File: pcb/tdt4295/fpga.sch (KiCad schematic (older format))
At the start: 45 parts, among them J101 FPGA__debug, U101 S25FL127SABMFV101, U102 XC7A100T-FTG256-tdt4295

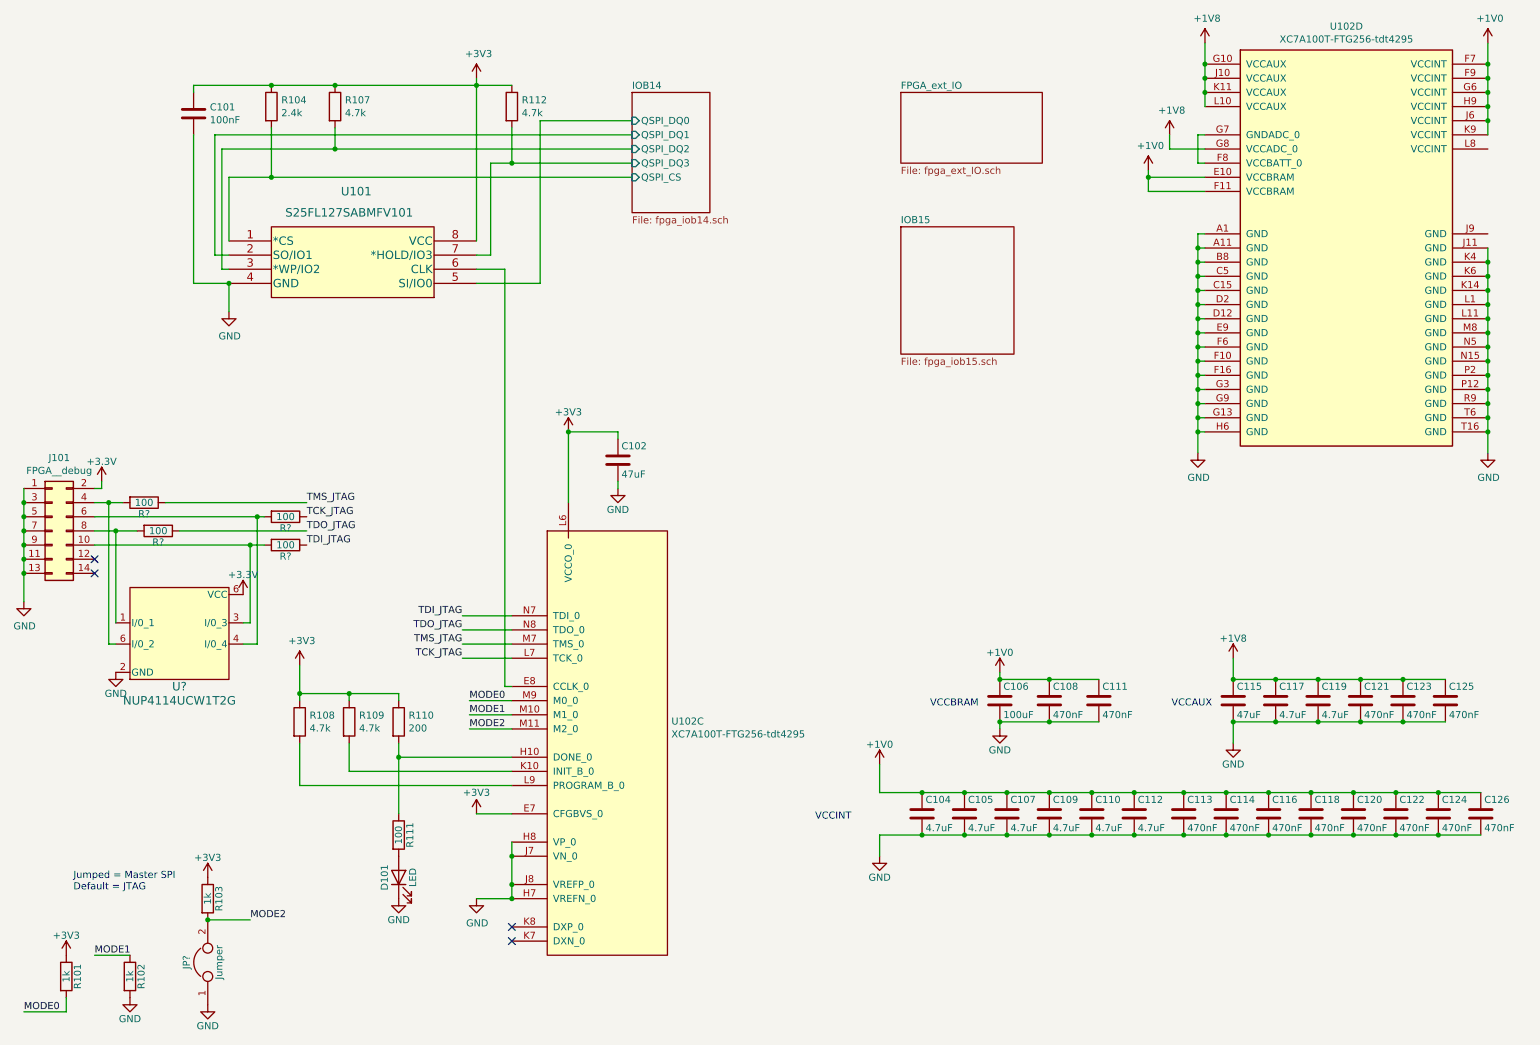
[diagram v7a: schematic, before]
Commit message: associate (some) footprints to the symbols
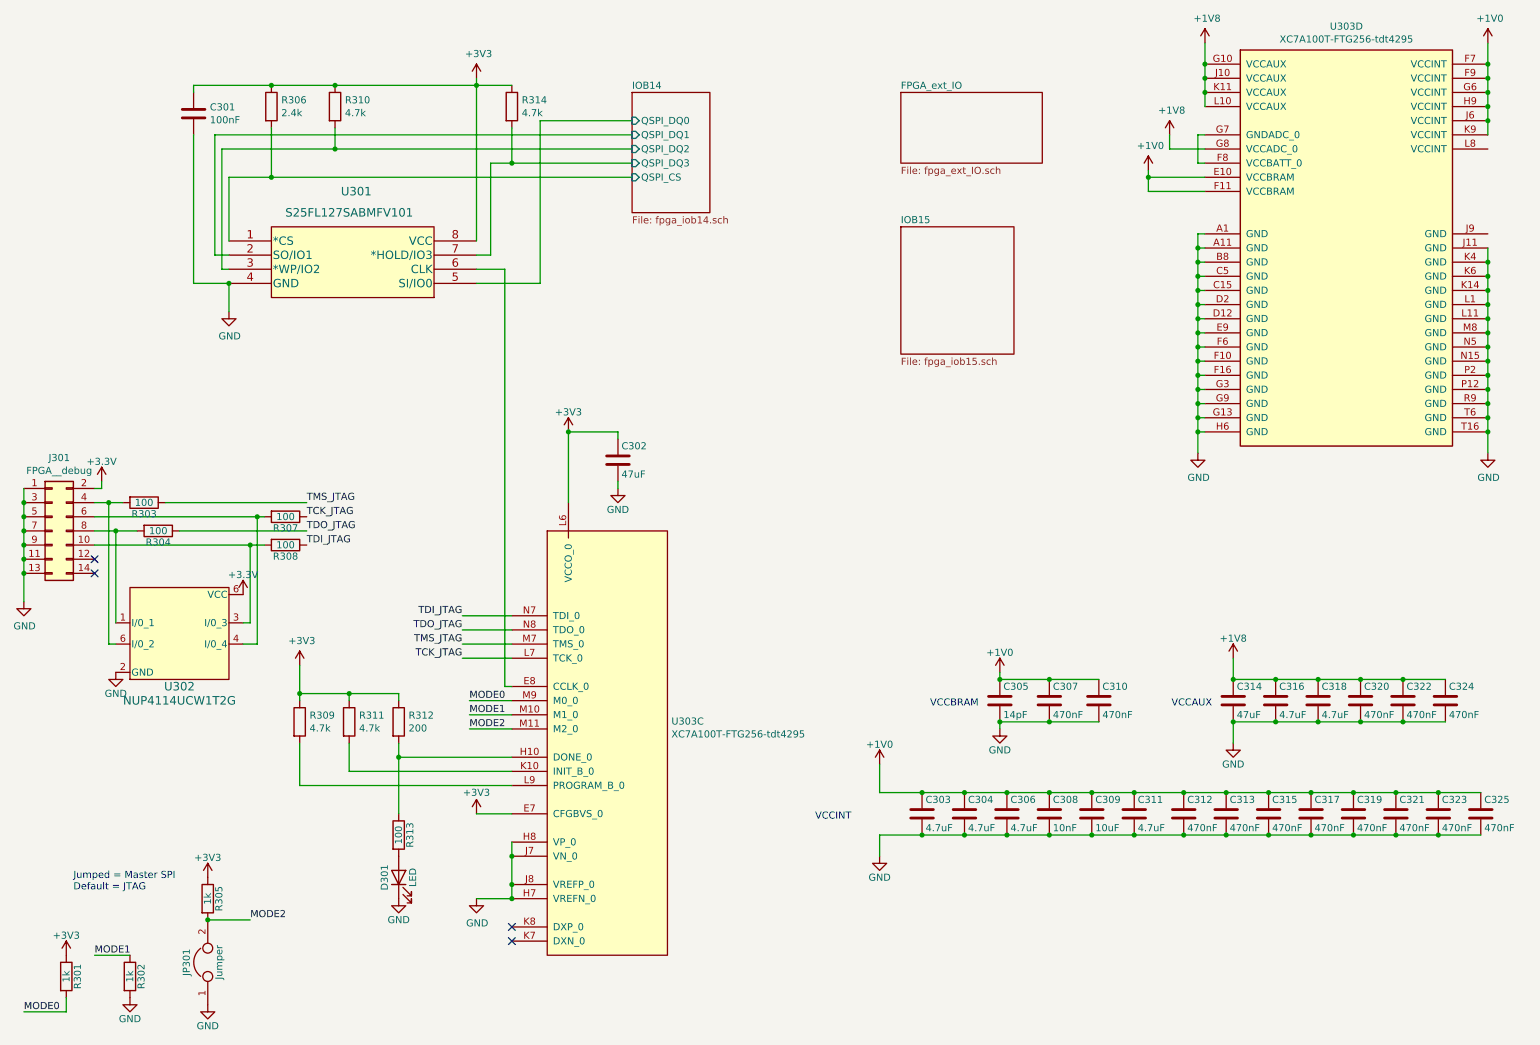
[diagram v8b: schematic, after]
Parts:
- C302: renamed from C102; DK_Detail_Page (none) -> https://www.digikey.no/product-detail/no/murata-electronics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
- C303: renamed from C104; Component name (none) -> C2012X7R1A475K125AC; DK_Detail_Page (none) -> https://www.digikey.no/product-detail/no/tdk-corporation/C2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
- C304: renamed from C105; Component name (none) -> C2012X7R1A475K125AC; DK_Detail_Page (none) -> https://www.digikey.no/product-detail/no/tdk-corporation/C2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
- C305: renamed from C106; value 100uF -> 14pF; Component name (none) -> C1210C107M9PACTU; DK_Detail_Page (none) -> https://no.farnell.com/kemet/c1210c107m9pactu/cap-100-f-6-3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
- C306: renamed from C107; Component name (none) -> C2012X7R1A475K125AC; DK_Detail_Page (none) -> https://www.digikey.no/product-detail/no/tdk-corporation/C2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
- C308: renamed from C109; value 4.7uF -> 10nF
- C309: renamed from C110; value 4.7uF -> 10uF
- C311: renamed from C112; Component name (none) -> C2012X7R1A475K125AC; DK_Detail_Page (none) -> https://www.digikey.no/product-detail/no/tdk-corporation/C2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
- C314: renamed from C115; Component name (none) -> GRM32ER71A476ME15L; DK_Detail_Page (none) -> https://www.digikey.no/product-detail/no/murata-electronics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
- C316: renamed from C117; Component name (none) -> C2012X7R1A475K125AC; DK_Detail_Page (none) -> https://www.digikey.no/product-detail/no/tdk-corporation/C2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
- C318: renamed from C119; Component name (none) -> C2012X7R1A475K125AC; DK_Detail_Page (none) -> https://www.digikey.no/product-detail/no/tdk-corporation/C2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
- R301: renamed from R101; DK_Detail_Page (none) -> https://www.digikey.no/product-detail/no/susumu/RR0510P-102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
- R302: renamed from R102; DK_Detail_Page (none) -> https://www.digikey.no/product-detail/no/susumu/RR0510P-102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
- R303, R304, R307, R308: renamed from R?; footprint (none) -> Resistor_SMD:R_0805_2012Metric_Pad1.20x1.40mm_HandSolder; Category (none) -> MCU08050C1000FP500; DK_Detail_Page (none) -> https://www.digikey.no/product-detail/no/vishay-beyschlag-d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
- R305: renamed from R103; DK_Detail_Page (none) -> https://www.digikey.no/product-detail/no/susumu/RR0510P-102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
- R306: renamed from R104; DK_Detail_Page (none) -> https://www.digikey.no/product-detail/no/panasonic-electron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
- R309: renamed from R108; DK_Detail_Page (none) -> https://www.digikey.no/product-detail/no/susumu/RG1608P-472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
- R310: renamed from R107; DK_Detail_Page (none) -> https://www.digikey.no/product-detail/no/susumu/RG1608P-472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
- R311: renamed from R109; DK_Detail_Page (none) -> https://www.digikey.no/product-detail/no/susumu/RG1608P-472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
- R312: renamed from R110; DK_Detail_Page (none) -> https://www.digikey.no/product-detail/no/stackpole-electron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
- R313: renamed from R111; DK_Detail_Page (none) -> https://www.digikey.no/product-detail/no/vishay-dale/TNPW08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
- R314: renamed from R112; DK_Detail_Page (none) -> https://www.digikey.no/product-detail/no/susumu/RG1608P-472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
- gave numbers to parts that had none: 2
- renumbered C101 to C301, C108 to C307, C111 to C310, C113 to C312, C114 to C313, C116 to C315, C118 to C317, C120 to C319, C121 to C320, C122 to C321, C123 to C322, C124 to C323, C125 to C324, C126 to C325, D101 to D301, J101 to J301, U101 to U301, U102 to U303
